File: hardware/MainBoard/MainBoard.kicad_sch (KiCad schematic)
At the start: 49 parts, among them J1 Conn_01x08_Socket, J2 Conn_01x08_Socket, J3 Conn_01x08_Socket, J4 Micro_SD_Card_Det2, J5 USB_C_Receptacle_USB2.0_16P, J8 En_A, J9 En_B, Q1 MMBT2222A, U1 ESP32-S3-WROOM-1, U2 AMS1117-3.3, U3 AMS1117-5.0

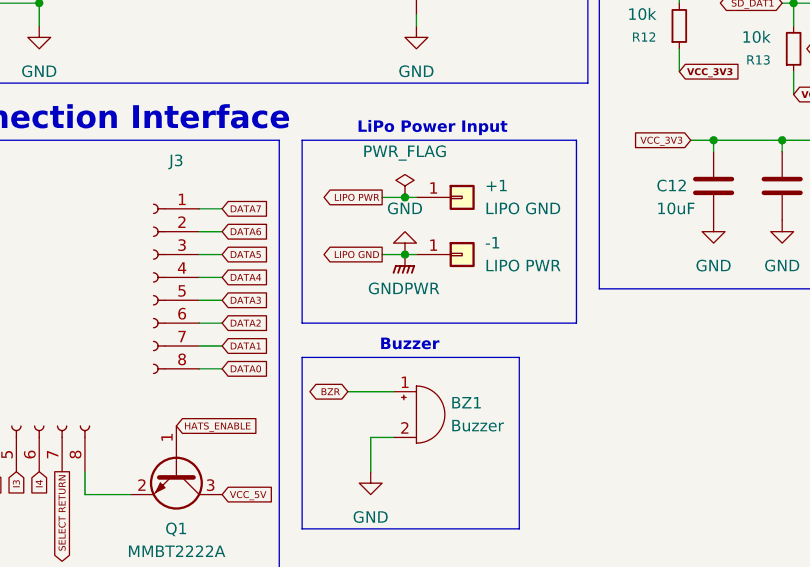
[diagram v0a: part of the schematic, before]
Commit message: added power flag to ground
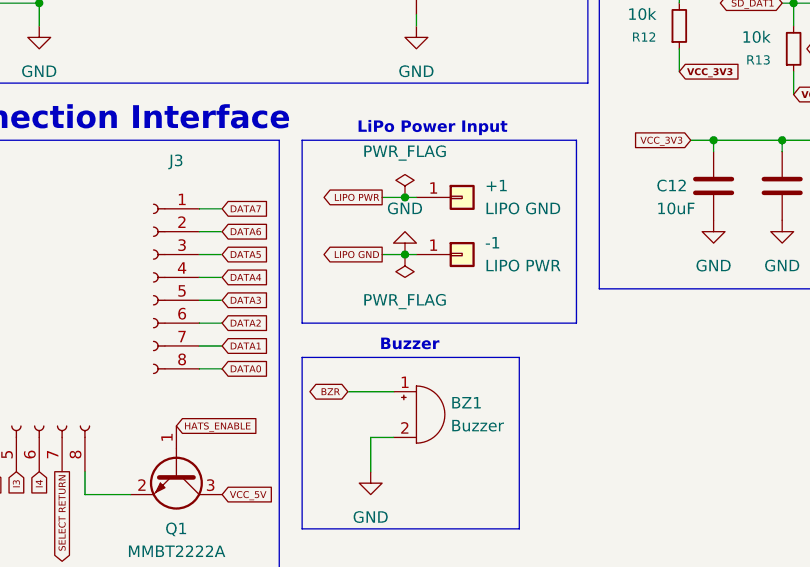
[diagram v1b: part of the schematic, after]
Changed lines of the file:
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@@
-	)
-	(symbol
-		(lib_id "power:GNDPWR")
-		(at 158.75 118.11 0)
-		(unit 1)
-		(exclude_from_sim no)
-		(in_bom yes)
-		(on_board yes)
-		(dnp no)
-		(fields_autoplaced yes)
-		(property "Reference" "#PWR013"
-			(at 158.75 123.19 0)
-			(effects
-				(font
-					(size 1.27 1.27)
-				)
-				(hide yes)
-			)
-		)
-		(property "Value" "GNDPWR"
-			(at 158.623 121.92 0)
-			(effects
-				(font
-					(size 1.27 1.27)
-				)
-			)
-		)
-		(property "Footprint" ""
-			(at 158.75 119.38 0)
-			(effects
-				(font
-					(size 1.27 1.27)
-				)
-				(hide yes)
-			)
-		)
-		(property "Datasheet" ""
-			(at 158.75 119.38 0)
-			(effects
-				(font
-					(size 1.27 1.27)
-				)
-				(hide yes)
-			)
-		)
-		(property "Description" "Power symbol creates a global label with name \"GNDPWR\" , global ground"
-			(at 158.75 118.11 0)
-			(effects
-				(font
-					(size 1.27 1.27)
-				)
-				(hide yes)
-			)
-		)
-		(pin "1"
-		)
-		(instances
-			(project ""
-				(path "/988df97c-fca1-40e2-af98-331e3f3f354f"
-					(reference "#PWR013")
-					(unit 1)
-				)
-			)
-		)
 	)
 	(symbol
@@
 					(unit 1)
 				)
+			)
+		)
+	)
+	(symbol
+		(lib_id "power:PWR_FLAG")
+		(at 158.75 118.11 180)
+		(unit 1)
+		(exclude_from_sim no)
+		(in_bom yes)
+		(on_board yes)
+		(dnp no)
+		(fields_autoplaced yes)
+		(property "Reference" "#FLG02"
+			(at 158.75 120.015 0)
+			(effects
+				(font
+					(size 1.27 1.27)
+				)
+				(hide yes)
+			)
+		)
+		(property "Value" "PWR_FLAG"
+			(at 158.75 123.19 0)
+			(effects
+				(font
+					(size 1.27 1.27)
+				)
+			)
+		)
+		(property "Footprint" ""
+			(at 158.75 118.11 0)
+			(effects
+				(font
+					(size 1.27 1.27)
+				)
+				(hide yes)
+			)
+		)
+		(property "Datasheet" "~"
+			(at 158.75 118.11 0)
+			(effects
+				(font
+					(size 1.27 1.27)
+				)
+				(hide yes)
+			)
+		)
+		(property "Description" "Special symbol for telling ERC where power comes from"
+			(at 158.75 118.11 0)
+			(effects
+				(font
+					(size 1.27 1.27)
+				)
+				(hide yes)
+			)
+		)
+		(pin "1"
+		)
+		(instances
+			(project ""
+				(path "/988df97c-fca1-40e2-af98-331e3f3f354f"
+					(reference "#FLG02")
+					(unit 1)
+				)

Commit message: main boards almost done:
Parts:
- removed J1, J2, J3: Conn_01x08_Socket, Connector_PinSocket_2.54mm:PinSocket_1x08_P2.54mm_Vertical, symbol Connector:Conn_01x08_Socket
- added Hat_Conn1, Plug1, Recepticle1: Conn_02x15_Top_Bottom, Connector_Molex:Molex_SlimStack_53748-0308_2x15_P0.50mm_Vertical, symbol Connector_Generic:Conn_02x15_Top_Bottom
- added J1, J2: Conn_01x01, TestPoint:TestPoint_Pad_1.5x1.5mm, symbol Connector_Generic:Conn_01x01
- +1, -1: footprint TestPoint:TestPoint_Pad_4.0x4.0mm -> TestPoint:TestPoint_Pad_2.0x2.0mm
- BZ1: footprint Buzzer_Beeper:MagneticBuzzer_Kingstate_KCG0601 -> Buzzer_Beeper:Buzzer_Murata_PKMCS0909E
- C1, C10, C12, C15, C2, C4, C8: footprint Capacitor_SMD:C_0805_2012Metric -> Capacitor_SMD:C_0603_1608Metric
- D2, D3, D4: footprint Diode_SMD:D_0805_2012Metric -> Diode_SMD:D_0603_1608Metric
- Q1: footprint Package_TO_SOT_SMD:SOT-23W_Handsoldering -> Package_TO_SOT_SMD:SOT-23W
- R1, R2: footprint Resistor_SMD:R_1206_3216Metric -> Resistor_SMD:R_0402_1005Metric
- R10, R12, R13, R3, R4, R5, R6, R7, R8, R9: footprint Resistor_SMD:R_1206_3216Metric -> Resistor_SMD:R_0603_1608Metric
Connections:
- net CONN_5V: now reaches Q1.2 (E)
- net CONN_5V: now also J1.1 (Pin_1)
- net DATA0: no longer names the net of U1.4 (IO4)
- net DATA1: no longer names the net of U1.5 (IO5)
- net DATA10: no longer names the net of U1.9 (IO16)
- net DATA11: no longer names the net of U1.10 (IO17)
- net DATA12: no longer names the net of U1.11 (IO18)
- net DATA13: no longer names the net of U1.12 (IO8)
- net DATA14: no longer names the net of U1.15 (IO3)
- net DATA15: no longer names the net of U1.16 (IO46)
- net DATA2: no longer names the net of U1.6 (IO6)
- net DATA3: no longer names the net of U1.39 (IO1)
- net DATA4: no longer names the net of U1.38 (IO2)
- net DATA5: no longer names the net of U1.37 (TXD0)
- net DATA6: no longer names the net of U1.36 (RXD0)
- net DATA7: no longer names the net of U1.35 (IO42)
- net DATA8: no longer names the net of U1.7 (IO7)
- net DATA9: no longer names the net of U1.8 (IO15)
- net ESP_3V3 renamed CONN_26
- net CONN_26: now also Plug1.28 (Pin_28), Plug1.30 (Pin_30), Recepticle1.27 (Pin_27), Recepticle1.29 (Pin_29)
- net HATS_ENABLE renamed CONN_12
- net CONN_12: now also Plug1.14 (Pin_14), Recepticle1.13 (Pin_13)
- net I0: no longer names the net of U1.26 (IO45)
- net I1: no longer names the net of U1.25 (IO48)
- net I2: no longer names the net of U1.24 (IO47)
- net I3: no longer names the net of U1.23 (IO21)
- net I4: no longer names the net of U1.22 (IO14)
- net SD_CLK renamed CONN_4
- net CONN_4: now also Plug1.6 (Pin_6), Recepticle1.5 (Pin_5)
- net SD_CMD renamed CONN_6
- net CONN_6: now also Plug1.8 (Pin_8), Recepticle1.7 (Pin_7)
- net SD_DAT0 renamed CONN_2
- net CONN_2: now also Plug1.4 (Pin_4), Recepticle1.3 (Pin_3)
- net SD_DAT1 renamed CONN_0
- net CONN_0: now also Plug1.2 (Pin_2), Recepticle1.1 (Pin_1)
- net SD_DAT2 renamed CONN_10
- net CONN_10: now also Plug1.12 (Pin_12), Recepticle1.11 (Pin_11)
- net SD_DAT3 renamed CONN_8
- net CONN_8: now also Plug1.10 (Pin_10), Recepticle1.9 (Pin_9)
- net SELECT RETURN renamed RET
- net RET: now also Plug1.29 (Pin_29), Recepticle1.30 (Pin_30)
- net USB+ renamed CONN_3
- net CONN_3: now also Plug1.3 (Pin_3), Recepticle1.4 (Pin_4)
- net USB- renamed CONN_1
- net CONN_1: now also Plug1.1 (Pin_1), Recepticle1.2 (Pin_2)
- new net CONN_11: Plug1.11 (Pin_11), Recepticle1.12 (Pin_12)
- new net CONN_13: Plug1.13 (Pin_13), Recepticle1.14 (Pin_14)
- new net CONN_14: Plug1.16 (Pin_16), Recepticle1.15 (Pin_15)
- new net CONN_15: Plug1.15 (Pin_15), Recepticle1.16 (Pin_16)
- new net CONN_16: Plug1.18 (Pin_18), Recepticle1.17 (Pin_17)
- new net CONN_17: Plug1.17 (Pin_17), Recepticle1.18 (Pin_18)
- new net CONN_18: Plug1.20 (Pin_20), Recepticle1.19 (Pin_19)
- new net CONN_19: Plug1.19 (Pin_19), Recepticle1.20 (Pin_20)
- new net CONN_20: Plug1.22 (Pin_22), Recepticle1.21 (Pin_21)
- new net CONN_21: Plug1.21 (Pin_21), Recepticle1.22 (Pin_22)
- new net CONN_22: Plug1.24 (Pin_24), Recepticle1.23 (Pin_23)
- new net CONN_23: Plug1.23 (Pin_23), Recepticle1.24 (Pin_24)
- new net CONN_24: Plug1.26 (Pin_26), Recepticle1.25 (Pin_25)
- new net CONN_25: Plug1.25 (Pin_25), Recepticle1.26 (Pin_26)
- new net CONN_27: Plug1.27 (Pin_27), Recepticle1.28 (Pin_28)
- new net CONN_5: Plug1.5 (Pin_5), Recepticle1.6 (Pin_6)
- new net CONN_7: Plug1.7 (Pin_7), Recepticle1.8 (Pin_8)
- new net CONN_9: Plug1.9 (Pin_9), Recepticle1.10 (Pin_10)
- new net CONN_GND: J2.1 (Pin_1)
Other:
- note added: "This is ordered weirdly bc of the pinout and the connectors being on opposite faces"
- note added: "these are the power and ground rails on the hat connector"
- moved on the sheet: Q1

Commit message: started wiring main boards
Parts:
- removed BOOT1: RESET, Button_Switch_SMD:SW_Push_1P1T_NO_CK_KMR2, symbol Switch:SW_Push
- removed BZ1: Buzzer, Buzzer_Beeper:Buzzer_Murata_PKMCS0909E, symbol Device:Buzzer
- removed C1, C12: 10uF, Capacitor_SMD:C_0603_1608Metric, symbol Device:C
- removed C13: 100nF, Capacitor_SMD:C_0402_1005Metric, symbol Device:C
- removed C6, C7: 0u1F, Capacitor_SMD:C_0402_1005Metric, symbol Device:C
- removed D1: 1N5819WS, Diode_SMD:D_SOD-323, symbol Diode:1N5819WS
- removed D2, D3, D4: D_TVS_Small_Filled, Diode_SMD:D_0603_1608Metric, symbol Device:D_TVS_Small_Filled
- removed J4: Micro_SD_Card_Det2, Connector_Card:microSD_HC_Hirose_DM3AT-SF-PEJM5, symbol Connector:Micro_SD_Card_Det2
- removed J5: USB_C_Receptacle_USB2.0_16P, Connector_USB:USB_C_Receptacle_GCT_USB4085, symbol Connector:USB_C_Receptacle_USB2.0_16P
- removed R1, R2: 5k1, Resistor_SMD:R_0402_1005Metric, symbol Device:R
- removed R10, R12, R13, R8, R9: 10k, Resistor_SMD:R_0603_1608Metric, symbol Device:R_Small
- removed R4, R5: 10k, Resistor_SMD:R_0603_1608Metric, symbol Device:R
- added J10, J7: Conn_01x01, TestPoint:TestPoint_Pad_1.5x1.5mm, symbol Connector_Generic:Conn_01x01
- J8: value En_A -> Conn_01x01
- J9: value En_B -> Conn_01x01
- renumbered C14 to C1, C16 to C2, C15 to C3, C2 to C4, C3 to C5, C4 to C6, C5 to C7, D5 to D1, D6 to D2, R7 to R1, R3 to R2, R6 to R3
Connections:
- net CHIP_PU: no longer J9.1 (Pin_1)
- net CONN_27: now also Plug1.29 (Pin_29)
- net CONN_GND: now also J8.1 (Pin_1), J10.1 (Pin_1)
- net GPIO0: now also U1.39 (IO1); no longer U1.27 (IO0)
- net RET: now also Hat_Conn1.30 (Pin_30); no longer Plug1.29 (Pin_29)
- net LIPO PWR renamed CONN_3V
- net CONN_3V: now also J9.1 (Pin_1), J7.1 (Pin_1)
- no-connect marks 4 -> 2
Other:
- added sheet peripherals (peripherals.kicad_sch)
- note removed: "Buttons"
- note removed: "Buzzer"
- note removed: "SD Card"
- note removed: "USB-C"

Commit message: wide board lel
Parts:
- removed Hat_Conn1, Plug1, Recepticle1: Conn_02x15_Top_Bottom, Connector_Molex:Molex_SlimStack_53748-0308_2x15_P0.50mm_Vertical, symbol Connector_Generic:Conn_02x15_Top_Bottom
- removed J1, J10, J2, J7, J8, J9: Conn_01x01, TestPoint:TestPoint_Pad_1.5x1.5mm, symbol Connector_Generic:Conn_01x01
- added J1: Conn_02x16_Top_Bottom, MolexFSB:FSB5 Series 0.40 mm Pitch Floating SlimStack Board-to-Board Receptacles, symbol Connector_Generic:Conn_02x16_Top_Bottom
- added J2, J7: Conn_02x16_Top_Bottom, MolexFSB:FSB5 Series 0.40 mm Pitch Floating SlimStack Board-to-Board Plugs, symbol Connector_Generic:Conn_02x16_Top_Bottom
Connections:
- net RET is gone; now on net CONN_21: U1.21 (IO13)
- net CONN_0: now also J1.1 (Pin_1), J2.16 (Pin_16), J7.1 (Pin_1); no longer U1.34 (IO41)
- net CONN_1: now also J1.2 (Pin_2), J2.17 (Pin_17), J7.2 (Pin_2); no longer U1.13 (USB_D-)
- net CONN_10: now also J1.11 (Pin_11), J2.26 (Pin_26), J7.11 (Pin_11); no longer U1.28 (IO35)
- net CONN_11: now also J1.12 (Pin_12), J2.27 (Pin_27), J7.12 (Pin_12)
- net CONN_12: now also J1.13 (Pin_13), J2.28 (Pin_28), J7.13 (Pin_13); no longer Q1.1 (B), U1.20 (IO12)
- net CONN_13: now also J1.14 (Pin_14), J2.29 (Pin_29), J7.14 (Pin_14)
- net CONN_14: now also J1.15 (Pin_15), J7.15 (Pin_15)
- net CONN_15: now also J1.16 (Pin_16), J2.2 (Pin_2), J7.16 (Pin_16)
- net CONN_16: now also J1.17 (Pin_17), J2.1 (Pin_1)
- net CONN_17: now also J1.18 (Pin_18), J2.3 (Pin_3)
- net CONN_18: now also J1.19 (Pin_19), J2.4 (Pin_4)
- net CONN_19: now also J1.20 (Pin_20), J2.5 (Pin_5)
- net CONN_2: now also J1.3 (Pin_3), J2.18 (Pin_18), J7.3 (Pin_3); no longer U1.33 (IO40)
- net CONN_20: now also J1.21 (Pin_21), J2.6 (Pin_6)
- net CONN_21: now also J1.22 (Pin_22), J1.30 (Pin_30), J2.30 (Pin_30), J2.7 (Pin_7)
- net CONN_22: now also U1.13 (USB_D-), J1.23 (Pin_23), J2.8 (Pin_8)
- net CONN_23: now also U1.14 (USB_D+), J1.24 (Pin_24), J2.9 (Pin_9)
- net CONN_24: now also U1.28 (IO35), J1.25 (Pin_25), J2.10 (Pin_10)
- net CONN_25: now also U1.29 (IO36), J1.26 (Pin_26), J2.11 (Pin_11)
- net CONN_26: now also U1.30 (IO37), J1.27 (Pin_27), J2.12 (Pin_12); no longer C2.1, C3.1, C6.1, C7.1, R1.1, R2.1, U1.2 (3V3), U2.2 (VO)
- net CONN_27: now also U1.32 (IO39), J1.28 (Pin_28), J2.13 (Pin_13)
- net CONN_3: now also J1.4 (Pin_4), J2.19 (Pin_19), J7.4 (Pin_4); no longer U1.14 (USB_D+)
- net CONN_4: now also J1.5 (Pin_5), J2.20 (Pin_20), J7.5 (Pin_5); no longer U1.32 (IO39)
- net CONN_5: now also J1.6 (Pin_6), J2.21 (Pin_21), J7.6 (Pin_6)
- net CONN_6: now also J1.7 (Pin_7), J2.22 (Pin_22), J7.7 (Pin_7); no longer U1.30 (IO37)
- net CONN_7: now also J1.8 (Pin_8), J2.23 (Pin_23), J7.8 (Pin_8)
- net CONN_8: now also J1.9 (Pin_9), J2.24 (Pin_24), J7.9 (Pin_9); no longer U1.29 (IO36)
- net CONN_9: now also J1.10 (Pin_10), J2.25 (Pin_25), J7.10 (Pin_10)
- net GND: now also J1.32 (Pin_32), J2.32 (Pin_32)
- net GPIO0: now also U1.27 (IO0); no longer U1.39 (IO1)
- new net CONN_28: J1.29 (Pin_29), J2.14 (Pin_14), U1.33 (IO40)
- new net CONN_29: J2.15 (Pin_15), U1.34 (IO41)
- new net CONN_VCC: C2.1, C3.1, C6.1, C7.1, J1.31 (Pin_31), J2.31 (Pin_31), R1.1, R2.1, U1.2 (3V3), U2.2 (VO)
- new net HATS_ENABLE: Q1.1 (B), U1.20 (IO12)
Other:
- note removed: "This is ordered weirdly bc of the pinout and the connectors being on opposite faces"
- note removed: "these are the power and ground rails on the hat connector"
- moved on the sheet: Q1

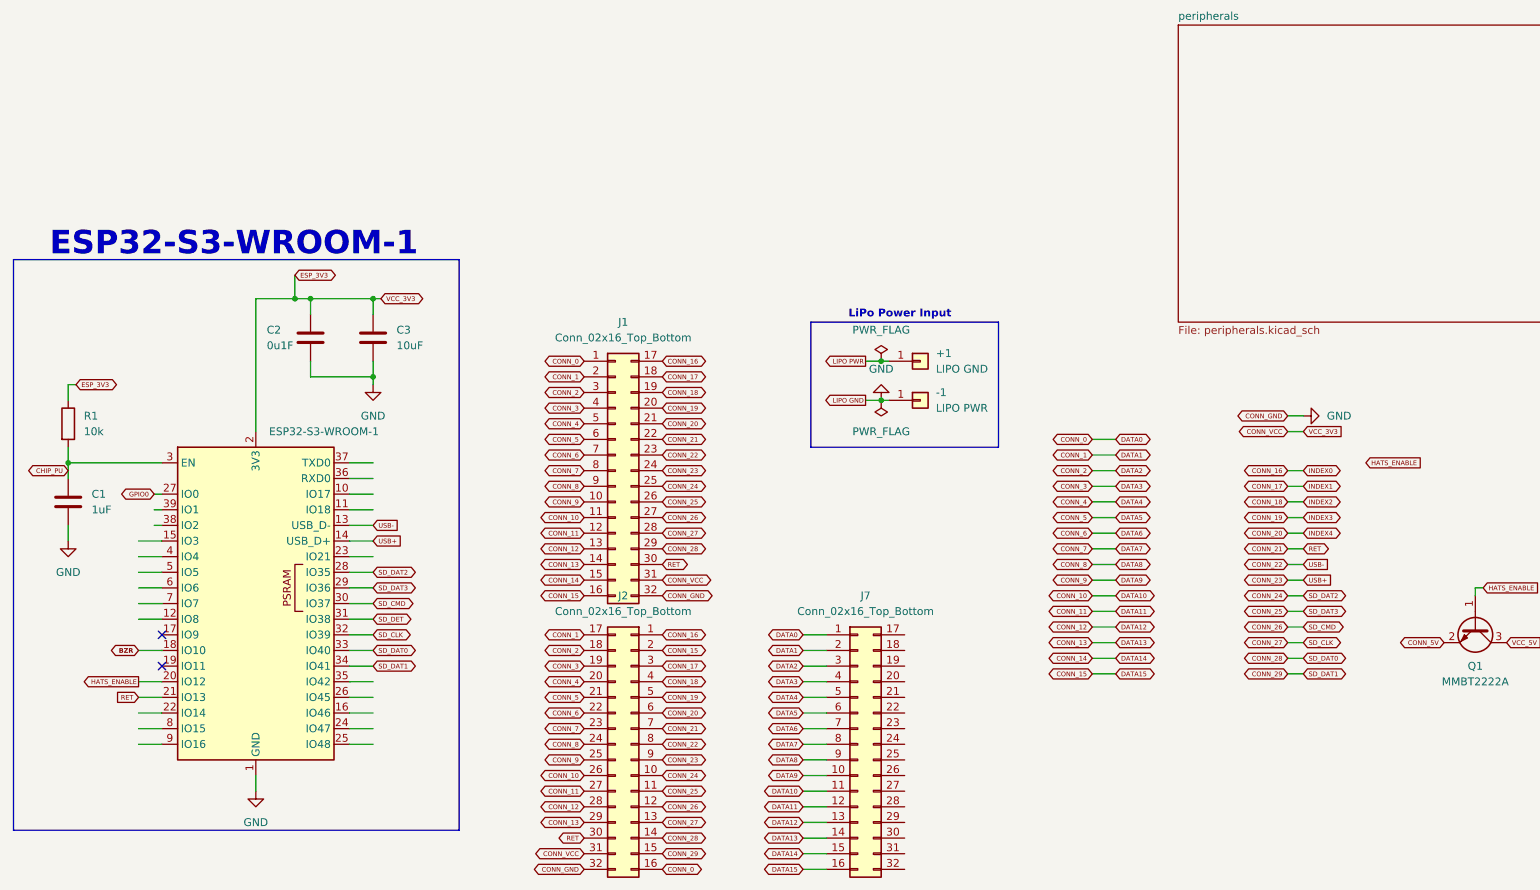
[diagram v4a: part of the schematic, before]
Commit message: started final traces
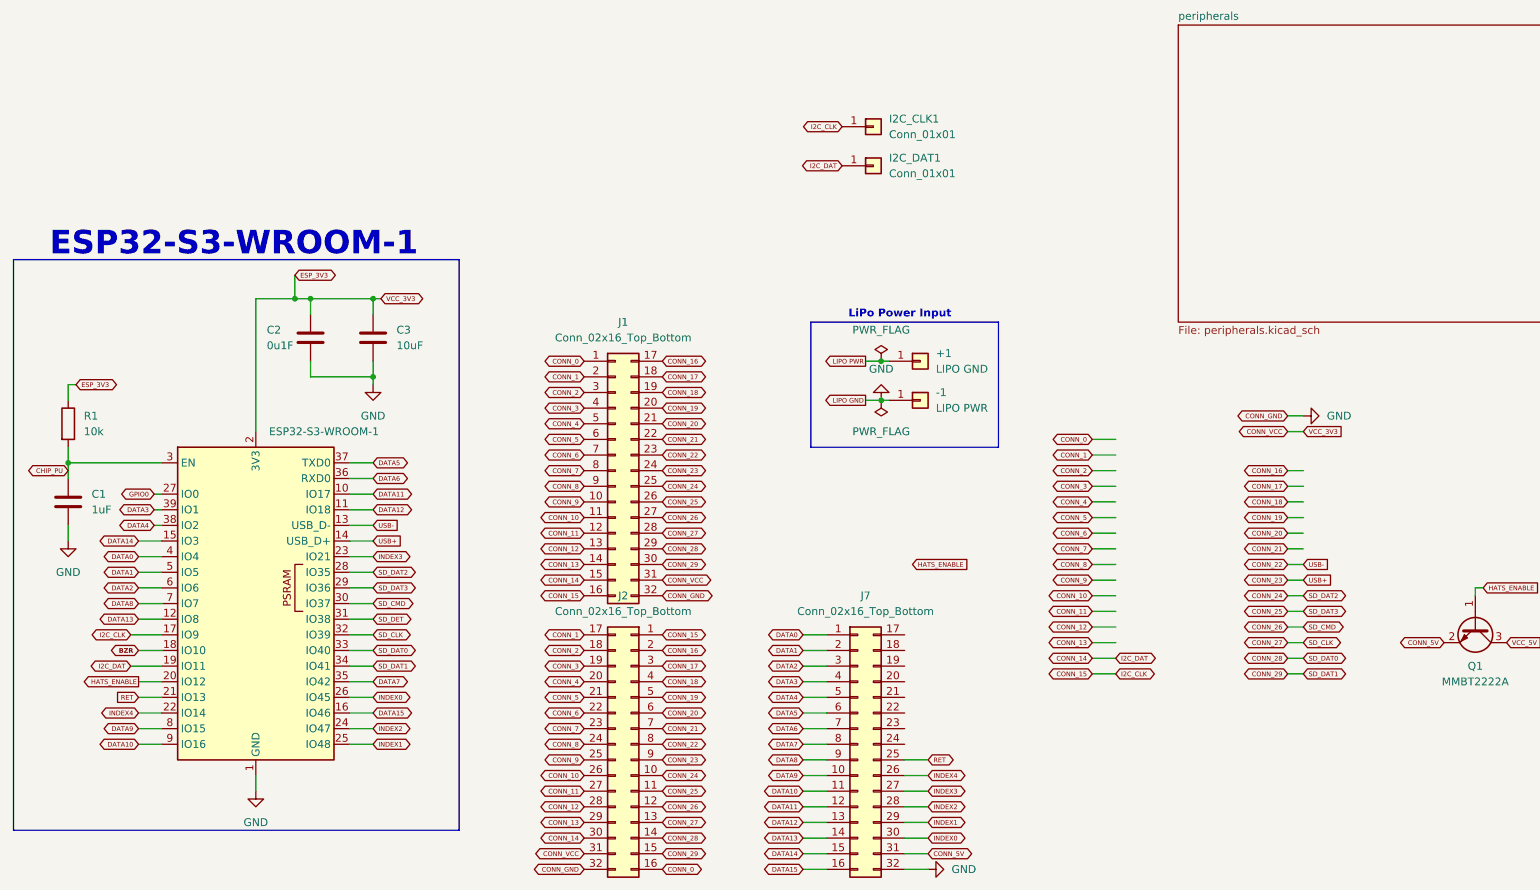
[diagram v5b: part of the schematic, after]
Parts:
- added I2C_CLK1, I2C_DAT1: Conn_01x01, TestPoint:TestPoint_Pad_1.0x1.0mm, symbol Connector_Generic:Conn_01x01
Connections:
- net CONN_0: no longer J7.1 (Pin_1)
- net CONN_1: no longer J7.2 (Pin_2)
- net CONN_10: no longer J7.11 (Pin_11)
- net CONN_11: no longer J7.12 (Pin_12)
- net CONN_12: no longer J7.13 (Pin_13)
- net CONN_13: no longer J7.14 (Pin_14)
- net CONN_14: now also J2.30 (Pin_30), U1.19 (IO11), I2C_DAT1.1 (Pin_1); no longer J7.15 (Pin_15)
- net CONN_15: now also J2.1 (Pin_1), U1.17 (IO9), I2C_CLK1.1 (Pin_1); no longer J2.2 (Pin_2), J7.16 (Pin_16)
- net CONN_16: now also J2.2 (Pin_2); no longer J2.1 (Pin_1)
- net CONN_2: no longer J7.3 (Pin_3)
- net CONN_21: no longer J1.30 (Pin_30), J2.30 (Pin_30), U1.21 (IO13)
- net CONN_29: now also J1.30 (Pin_30)
- net CONN_3: no longer J7.4 (Pin_4)
- net CONN_4: no longer J7.5 (Pin_5)
- net CONN_5: no longer J7.6 (Pin_6)
- net CONN_5V: now also J7.31 (Pin_31)
- net CONN_6: no longer J7.7 (Pin_7)
- net CONN_7: no longer J7.8 (Pin_8)
- net CONN_8: no longer J7.9 (Pin_9)
- net CONN_9: no longer J7.10 (Pin_10)
- net GND: now also J7.32 (Pin_32)
- net RET: now reaches J7.25 (Pin_25)
- net RET: now also U1.21 (IO13)
- net INDEX4: now reaches J7.26 (Pin_26)
- net INDEX4: now also U1.22 (IO14)
- net INDEX3: now reaches J7.27 (Pin_27)
- net INDEX3: now also U1.23 (IO21)
- net INDEX2: now reaches J7.28 (Pin_28)
- net INDEX2: now also U1.24 (IO47)
- net INDEX1: now reaches J7.29 (Pin_29)
- net INDEX1: now also U1.25 (IO48)
- net INDEX0: now reaches J7.30 (Pin_30)
- net INDEX0: now also U1.26 (IO45)
- net DATA11: now reaches U1.10 (IO17)
- net DATA11: now also J7.12 (Pin_12)
- net DATA12: now reaches U1.11 (IO18)
- net DATA12: now also J7.13 (Pin_13)
- net DATA13: now reaches U1.12 (IO8)
- net DATA13: now also J7.14 (Pin_14)
- net DATA14: now reaches U1.15 (IO3)
- net DATA14: now also J7.15 (Pin_15)
- net DATA15: now reaches U1.16 (IO46)
- net DATA15: now also J7.16 (Pin_16)
- net DATA7: now reaches U1.35 (IO42)
- net DATA7: now also J7.8 (Pin_8)
- net DATA6: now reaches U1.36 (RXD0)
- net DATA6: now also J7.7 (Pin_7)
- net DATA5: now reaches U1.37 (TXD0)
- net DATA5: now also J7.6 (Pin_6)
- net DATA4: now reaches U1.38 (IO2)
- net DATA4: now also J7.5 (Pin_5)
- net DATA3: now reaches U1.39 (IO1)
- net DATA3: now also J7.4 (Pin_4)
- net DATA0: now reaches U1.4 (IO4)
- net DATA0: now also J7.1 (Pin_1)
- net DATA1: now reaches U1.5 (IO5)
- net DATA1: now also J7.2 (Pin_2)
- net DATA2: now reaches U1.6 (IO6)
- net DATA2: now also J7.3 (Pin_3)
- net DATA8: now reaches U1.7 (IO7)
- net DATA8: now also J7.9 (Pin_9)
- net DATA9: now reaches U1.8 (IO15)
- net DATA9: now also J7.10 (Pin_10)
- net DATA10: now reaches U1.9 (IO16)
- net DATA10: now also J7.11 (Pin_11)
- no-connect marks 2 -> 0
